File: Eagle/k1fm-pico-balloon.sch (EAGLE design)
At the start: 40 parts, among them Q1 ASTX-H11-25.000MHZ-T, Q2 DMP2305U, Q3 DMP2305U, U1 ATMEGA328, U2 Si5351A-B-GT, U3 MCP1754X-XXXXX/C, U4 TMP36, Y1 8/16/20MHz

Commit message: 4 Layers. Added external SCL, SDA, GPS lines.
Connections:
- new net B0: GPS1.4_TIMEPULSE, U1.PB0(ICP)
- new net D7: U1.PD7(AIN1), U2.CLK2
- net 3V: no longer J3.2
- net GND: no longer J3.1
- net SCL: now also J3.2
- net SDA: now also J3.1
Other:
- note added: "K1FM Pico Balloon 1.3"
- note removed: "K1FM Pico Balloon 1.2"
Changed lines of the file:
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@@
 <?xml version="1.0" encoding="utf-8"?>
 <!DOCTYPE eagle SYSTEM "eagle.dtd">
-<eagle version="9.2.2">
+<eagle version="9.4.1">
 <drawing>
 <settings>
@@
 <sheet>
 <plain>
-<text x="203.2" y="10.16" size="7.62" layer="94">K1FM Pico Balloon 1.2</text>
+<text x="203.2" y="10.16" size="7.62" layer="94">K1FM Pico Balloon 1.3</text>
 </plain>
 <instances>
@@
 </segment>
 <segment>
-<wire x1="38.1" y1="78.74" x2="40.64" y2="78.74" width="0.1524" layer="91"/>
-<label x="40.64" y="78.74" size="1.27" layer="95" xref="yes"/>
-<pinref part="J3" gate="G$1" pin="1"/>
-</segment>
-<segment>
 <pinref part="GPS-ANT" gate="G$1" pin="1"/>
 <pinref part="GND12" gate="1" pin="GND"/>
@@
 </net>
 <net name="3V" class="0">
-<segment>
-<wire x1="38.1" y1="81.28" x2="40.64" y2="81.28" width="0.1524" layer="91"/>
-<label x="40.64" y="81.28" size="1.27" layer="95" xref="yes"/>
-<pinref part="J3" gate="G$1" pin="2"/>
-</segment>
 <segment>
 <pinref part="R4" gate="G$1" pin="1"/>
@@
 <label x="261.62" y="55.88" size="1.27" layer="95" rot="R180" xref="yes"/>
 </segment>
+<segment>
+<wire x1="38.1" y1="78.74" x2="40.64" y2="78.74" width="0.1524" layer="91"/>
+<label x="40.64" y="78.74" size="1.27" layer="95" xref="yes"/>
+<pinref part="J3" gate="G$1" pin="1"/>
+</segment>
 </net>
 <net name="SCL" class="0">
@@
 <label x="261.62" y="58.42" size="1.27" layer="95" rot="R180" xref="yes"/>
 </segment>
+<segment>
+<wire x1="38.1" y1="81.28" x2="40.64" y2="81.28" width="0.1524" layer="91"/>
+<label x="40.64" y="81.28" size="1.27" layer="95" xref="yes"/>
+<pinref part="J3" gate="G$1" pin="2"/>
+</segment>
 </net>
 <net name="CLK0" class="0">
 <segment>
 <pinref part="U2" gate="G$1" pin="CLK0"/>
-<wire x1="289.56" y1="66.04" x2="292.1" y2="66.04" width="0.1524" layer="91"/>
-<label x="292.1" y="66.04" size="1.778" layer="95" xref="yes"/>
+<wire x1="289.56" y1="66.04" x2="294.64" y2="66.04" width="0.1524" layer="91"/>
+<wire x1="294.64" y1="66.04" x2="294.64" y2="68.58" width="0.1524" layer="91"/>
+<label x="294.64" y="68.58" size="1.778" layer="95" rot="R90" xref="yes"/>
 </segment>
 <segment>
@@
 </segment>
 </net>
+<net name="B0" class="0">
+<segment>
+<pinref part="U1" gate="G$1" pin="PB0(ICP)"/>
+<wire x1="157.48" y1="68.58" x2="160.02" y2="68.58" width="0.1524" layer="91"/>
+<label x="160.02" y="68.58" size="1.778" layer="95" xref="yes"/>
+</segment>
+<segment>
+<pinref part="GPS1" gate="G$1" pin="4_TIMEPULSE"/>
+<wire x1="223.52" y1="149.86" x2="226.06" y2="149.86" width="0.1524" layer="91"/>
+<label x="226.06" y="149.86" size="1.778" layer="95" xref="yes"/>
+</segment>
+</net>
+<net name="D7" class="0">
+<segment>
+<pinref part="U1" gate="G$1" pin="PD7(AIN1)"/>
+<wire x1="157.48" y1="73.66" x2="160.02" y2="73.66" width="0.1524" layer="91"/>
+<label x="160.02" y="73.66" size="1.27" layer="95" xref="yes"/>
+</segment>
+<segment>
+<pinref part="U2" gate="G$1" pin="CLK2"/>
+<wire x1="289.56" y1="55.88" x2="292.1" y2="55.88" width="0.1524" layer="91"/>
+<label x="292.1" y="55.88" size="1.27" layer="95" xref="yes"/>
+</segment>
+</net>

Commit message: Reorganized TX/RX lines - Conn layout
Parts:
- added J1: I2C, SparkFun-Connectors:CONN_02
- J2: value (none) -> ICSP; device SparkFun-Connectors:6_PIN_SERIAL_TARGET -> SparkFun-Connectors:CONN_03X2FEMALE
- J3: value (none) -> SERIAL; device SparkFun-Connectors:CONN_06SILK_FEMALE_PTH -> SparkFun-Connectors:CONN_03
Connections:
- net B0 renamed TIMEP
- net D7 renamed CLK2
- removed net D3: GPS1.3_RXD1, U1.PD3(INT1)
- removed net D4: GPS1.2_TXD1, U1.PD4(XCK/T0)
- new net RXD: GPS1.2_TXD1, U1.PD0(RXD)
- new net TXD: GPS1.3_RXD1, U1.PD1(TXD)
- net 3V: now also J2.2; no longer J2.VCC
- net DTR: now also J3.1; no longer J2.DTR
- net GND: now also J2.6; no longer J2.CTS, J2.GND
- net MISO: now also J2.1; no longer J3.5
- net MOSI: now also J2.4; no longer J3.4
- net RESET: now also J2.5; no longer J3.6
- net RXI: now also J3.3, U1.PD3(INT1); no longer J2.TXO, U1.PD0(RXD)
- net SCK: now also J2.3; no longer J3.3
- net SCL: now also J1.2; no longer J3.2
- net SDA: now also J1.1; no longer J3.1
- net TXO: now also J3.2, U1.PD4(XCK/T0); no longer J2.RXI, U1.PD1(TXD)
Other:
- note added: "K1FM Pico Balloon 1.3 WORK IN PROGRESS"
- note removed: "K1FM Pico Balloon 1.3"
- moved on the sheet: C10, J2

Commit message: Add diode and connection for direct solar power
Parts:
- removed 3.3V: 3.3V, SparkFun-Connectors:CONN_02
- added D1: 1N4148X-TP, diode:DIODE-SOD523
- added J4: POWER, SparkFun-Connectors:CONN_03
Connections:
- new net N$3: D1.A, J4.3
- net GND: now also J4.2; no longer 3.3V.2
- net VDD: now also D1.C, J4.1; no longer 3.3V.1
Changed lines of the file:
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@@
 <part name="GND6" library="SparkFun" deviceset="GND" device=""/>
 <part name="C11" library="SparkFun-Capacitors" library_urn="urn:adsk.eagle:library:510" deviceset="0.1UF" device="-0603-25V-5%" package3d_urn="urn:adsk.eagle:package:37414/1" value="0.47uF"/>
-<part name="3.3V" library="SparkFun-Connectors" library_urn="urn:adsk.eagle:library:513" deviceset="CONN_02" device="" package3d_urn="urn:adsk.eagle:package:38039/1" value="3.3V"/>
 <part name="R3" library="SparkFun-Resistors" library_urn="urn:adsk.eagle:library:532" deviceset="4.7KOHM" device="-0603-1/10W-1%" package3d_urn="urn:adsk.eagle:package:39650/1" value="4.7k"/>
 <part name="R4" library="SparkFun-Resistors" library_urn="urn:adsk.eagle:library:532" deviceset="4.7KOHM" device="-0603-1/10W-1%" package3d_urn="urn:adsk.eagle:package:39650/1" value="4.7k"/>
@@
 <part name="J2" library="SparkFun-Connectors" library_urn="urn:adsk.eagle:library:513" deviceset="CONN_03X2" device="FEMALE" package3d_urn="urn:adsk.eagle:package:38016/1" value="ICSP"/>
 <part name="J3" library="SparkFun-Connectors" library_urn="urn:adsk.eagle:library:513" deviceset="CONN_03" device="" package3d_urn="urn:adsk.eagle:package:38063/1" value="SERIAL"/>
+<part name="D1" library="diode" library_urn="urn:adsk.eagle:library:210" deviceset="DIODE-" device="SOD523" package3d_urn="urn:adsk.eagle:package:43410/1" value="1N4148X-TP"/>
+<part name="J4" library="SparkFun-Connectors" library_urn="urn:adsk.eagle:library:513" deviceset="CONN_03" device="" package3d_urn="urn:adsk.eagle:package:38063/1" value="POWER"/>
 </parts>
 <sheets>
@@
 <attribute name="VALUE" x="306.324" y="48.641" size="1.778" layer="96" font="vector"/>
 </instance>
-<instance part="3.3V" gate="G$1" x="35.56" y="177.8" smashed="yes" rot="R270">
-<attribute name="VALUE" x="30.734" y="180.34" size="1.778" layer="96" font="vector" rot="R270"/>
-<attribute name="NAME" x="41.148" y="180.34" size="1.778" layer="95" font="vector" rot="R270"/>
-</instance>
 <instance part="R3" gate="G$1" x="172.72" y="111.76" smashed="yes" rot="R90">
 <attribute name="NAME" x="171.196" y="111.76" size="1.778" layer="95" font="vector" rot="R90" align="bottom-center"/>
@@
 <attribute name="VALUE" x="30.48" y="78.994" size="1.778" layer="96" font="vector"/>
 <attribute name="NAME" x="30.48" y="91.948" size="1.778" layer="95" font="vector"/>
+</instance>
+<instance part="D1" gate="G$1" x="27.94" y="177.8" smashed="yes" rot="R270">
+<attribute name="NAME" x="28.4226" y="175.26" size="1.778" layer="95" rot="R270"/>
+<attribute name="VALUE" x="25.6286" y="175.26" size="1.778" layer="96" rot="R270"/>
+</instance>
+<instance part="J4" gate="J$1" x="38.1" y="177.8" smashed="yes" rot="R270">
+<attribute name="VALUE" x="30.734" y="180.34" size="1.778" layer="96" font="vector" rot="R270"/>
+<attribute name="NAME" x="43.688" y="180.34" size="1.778" layer="95" font="vector" rot="R270"/>
 </instance>
 </instances>
@@
 <pinref part="GND1" gate="1" pin="GND"/>
 <wire x1="38.1" y1="167.64" x2="38.1" y2="170.18" width="0.1524" layer="91"/>
-<pinref part="3.3V" gate="G$1" pin="2"/>
+<pinref part="J4" gate="J$1" pin="2"/>
 </segment>
 <segment>
@@
 <segment>
 <wire x1="35.56" y1="167.64" x2="35.56" y2="170.18" width="0.1524" layer="91"/>
-<pinref part="3.3V" gate="G$1" pin="1"/>
-<label x="33.02" y="167.64" size="1.778" layer="95" rot="R180" xref="yes"/>
-<wire x1="33.02" y1="167.64" x2="35.56" y2="167.64" width="0.1524" layer="91"/>
+<label x="25.4" y="167.64" size="1.778" layer="95" rot="R180" xref="yes"/>
+<wire x1="25.4" y1="167.64" x2="27.94" y2="167.64" width="0.1524" layer="91"/>
+<pinref part="D1" gate="G$1" pin="C"/>
+<wire x1="27.94" y1="167.64" x2="35.56" y2="167.64" width="0.1524" layer="91"/>
+<wire x1="27.94" y1="175.26" x2="27.94" y2="167.64" width="0.1524" layer="91"/>
+<junction x="27.94" y="167.64"/>
+<pinref part="J4" gate="J$1" pin="1"/>
 </segment>
 <segment>
@@
 </segment>
 </net>
+<net name="N$3" class="0">
+<segment>
+<pinref part="D1" gate="G$1" pin="A"/>
+<wire x1="27.94" y1="180.34" x2="27.94" y2="185.42" width="0.1524" layer="91"/>
+<wire x1="27.94" y1="185.42" x2="48.26" y2="185.42" width="0.1524" layer="91"/>
+<wire x1="48.26" y1="185.42" x2="48.26" y2="167.64" width="0.1524" layer="91"/>
+<wire x1="48.26" y1="167.64" x2="40.64" y2="167.64" width="0.1524" layer="91"/>
+<pinref part="J4" gate="J$1" pin="3"/>
+<wire x1="40.64" y1="167.64" x2="40.64" y2="170.18" width="0.1524" layer="91"/>
+</segment>
+</net>

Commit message: Revert to classic hw/sw serial configuration
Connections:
- net RXD: now also J3.3; no longer GPS1.2_TXD1
- net RXI: now also GPS1.2_TXD1, U1.PD4(XCK/T0); no longer J3.3, U1.PD3(INT1)
- net TXD: now also J3.2; no longer GPS1.3_RXD1
- net TXO: now also GPS1.3_RXD1, U1.PD3(INT1); no longer J3.2, U1.PD4(XCK/T0)
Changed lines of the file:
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@@
-</segment>
-</net>
-<net name="TXO" class="0">
-<segment>
-<pinref part="U1" gate="G$1" pin="PD4(XCK/T0)"/>
-<wire x1="157.48" y1="81.28" x2="160.02" y2="81.28" width="0.1524" layer="91"/>
-<label x="160.02" y="81.28" size="1.27" layer="95" xref="yes"/>
-</segment>
-<segment>
-<pinref part="J3" gate="J$1" pin="2"/>
-<wire x1="40.64" y1="86.36" x2="43.18" y2="86.36" width="0.1524" layer="91"/>
-<label x="43.18" y="86.36" size="1.27" layer="95" xref="yes"/>
-</segment>
-</net>
-<net name="RXI" class="0">
-<segment>
-<pinref part="U1" gate="G$1" pin="PD3(INT1)"/>
-<wire x1="157.48" y1="83.82" x2="160.02" y2="83.82" width="0.1524" layer="91"/>
-<label x="160.02" y="83.82" size="1.27" layer="95" xref="yes"/>
-</segment>
-<segment>
-<pinref part="J3" gate="J$1" pin="3"/>
-<wire x1="40.64" y1="88.9" x2="43.18" y2="88.9" width="0.1524" layer="91"/>
-<label x="43.18" y="88.9" size="1.27" layer="95" xref="yes"/>
 </segment>
 </net>
@@
 </segment>
 <segment>
-<pinref part="GPS1" gate="G$1" pin="2_TXD1"/>
-<wire x1="223.52" y1="139.7" x2="226.06" y2="139.7" width="0.1524" layer="91"/>
-<label x="226.06" y="139.7" size="1.778" layer="95" xref="yes"/>
+<pinref part="J3" gate="J$1" pin="3"/>
+<wire x1="40.64" y1="88.9" x2="43.18" y2="88.9" width="0.1524" layer="91"/>
+<label x="43.18" y="88.9" size="1.27" layer="95" xref="yes"/>
 </segment>
 </net>
@@
 </segment>
 <segment>
-<wire x1="226.06" y1="144.78" x2="223.52" y2="144.78" width="0.1524" layer="91"/>
-<pinref part="GPS1" gate="G$1" pin="3_RXD1"/>
-<label x="226.06" y="144.78" size="1.778" layer="95" xref="yes"/>
+<pinref part="J3" gate="J$1" pin="2"/>
+<wire x1="40.64" y1="86.36" x2="43.18" y2="86.36" width="0.1524" layer="91"/>
+<label x="43.18" y="86.36" size="1.27" layer="95" xref="yes"/>
 </segment>
 </net>
@@
 </segment>
 </net>
+<net name="RXI" class="0">
+<segment>
+<pinref part="U1" gate="G$1" pin="PD4(XCK/T0)"/>
+<wire x1="157.48" y1="81.28" x2="160.02" y2="81.28" width="0.1524" layer="91"/>
+<label x="160.02" y="81.28" size="1.27" layer="95" xref="yes"/>
+</segment>
+<segment>
+<pinref part="GPS1" gate="G$1" pin="2_TXD1"/>
+<wire x1="223.52" y1="139.7" x2="226.06" y2="139.7" width="0.1524" layer="91"/>
+<label x="226.06" y="139.7" size="1.778" layer="95" xref="yes"/>
+</segment>
+</net>
+<net name="TXO" class="0">
+<segment>
+<pinref part="U1" gate="G$1" pin="PD3(INT1)"/>
+<wire x1="157.48" y1="83.82" x2="160.02" y2="83.82" width="0.1524" layer="91"/>
+<label x="160.02" y="83.82" size="1.27" layer="95" xref="yes"/>
+</segment>
+<segment>
+<pinref part="GPS1" gate="G$1" pin="3_RXD1"/>
+<wire x1="223.52" y1="144.78" x2="226.06" y2="144.78" width="0.1524" layer="91"/>
+<label x="226.06" y="144.78" size="1.778" layer="95" xref="yes"/>
+</segment>
+</net>

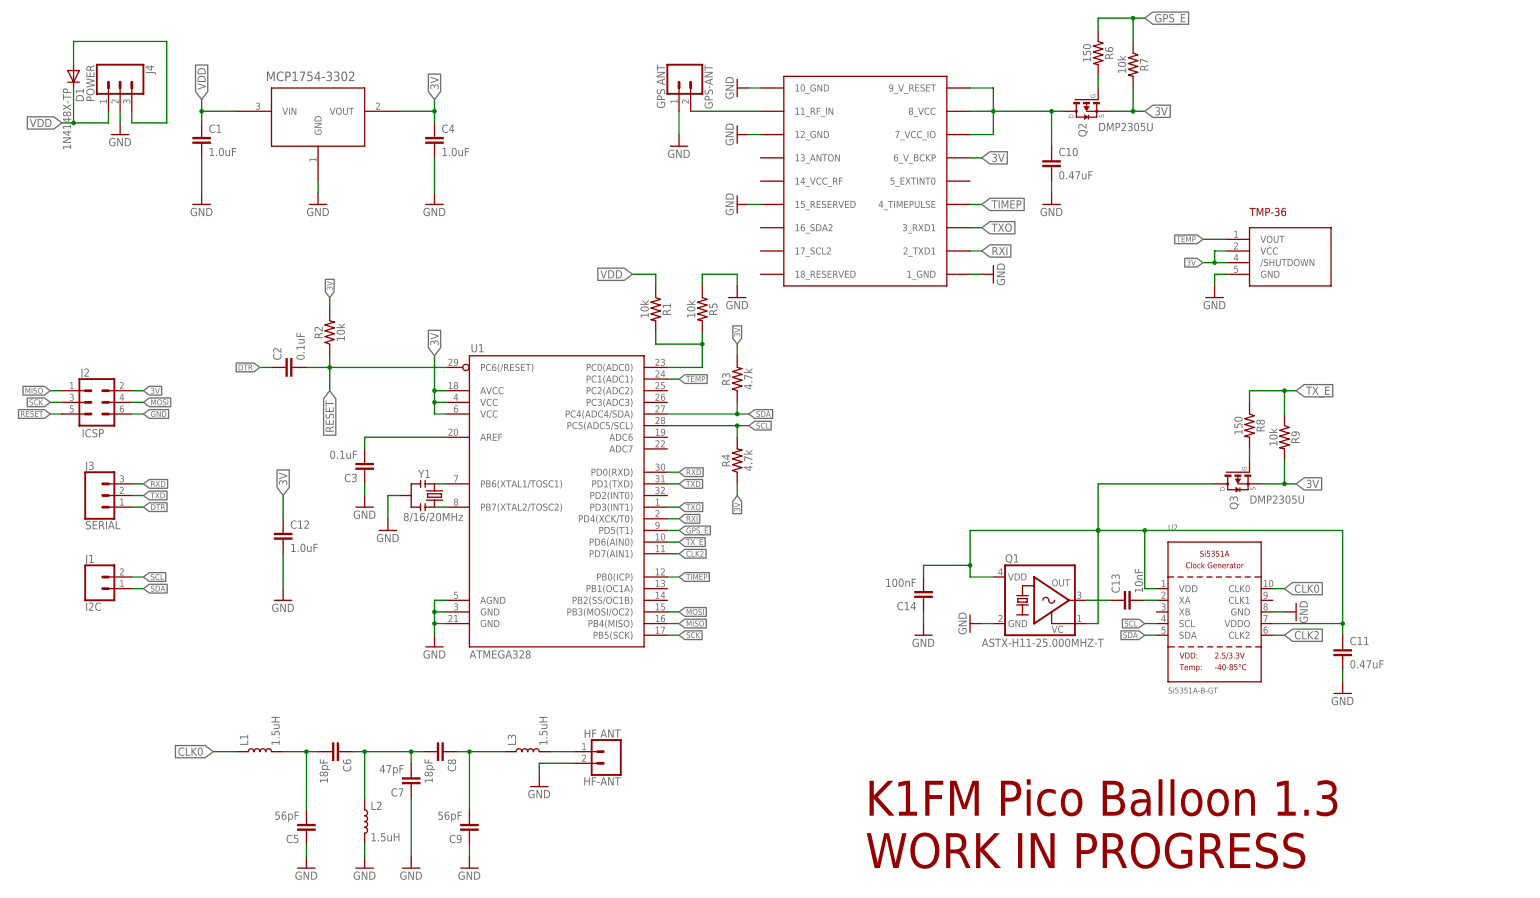
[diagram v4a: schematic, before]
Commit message: Redraw VDD measure input
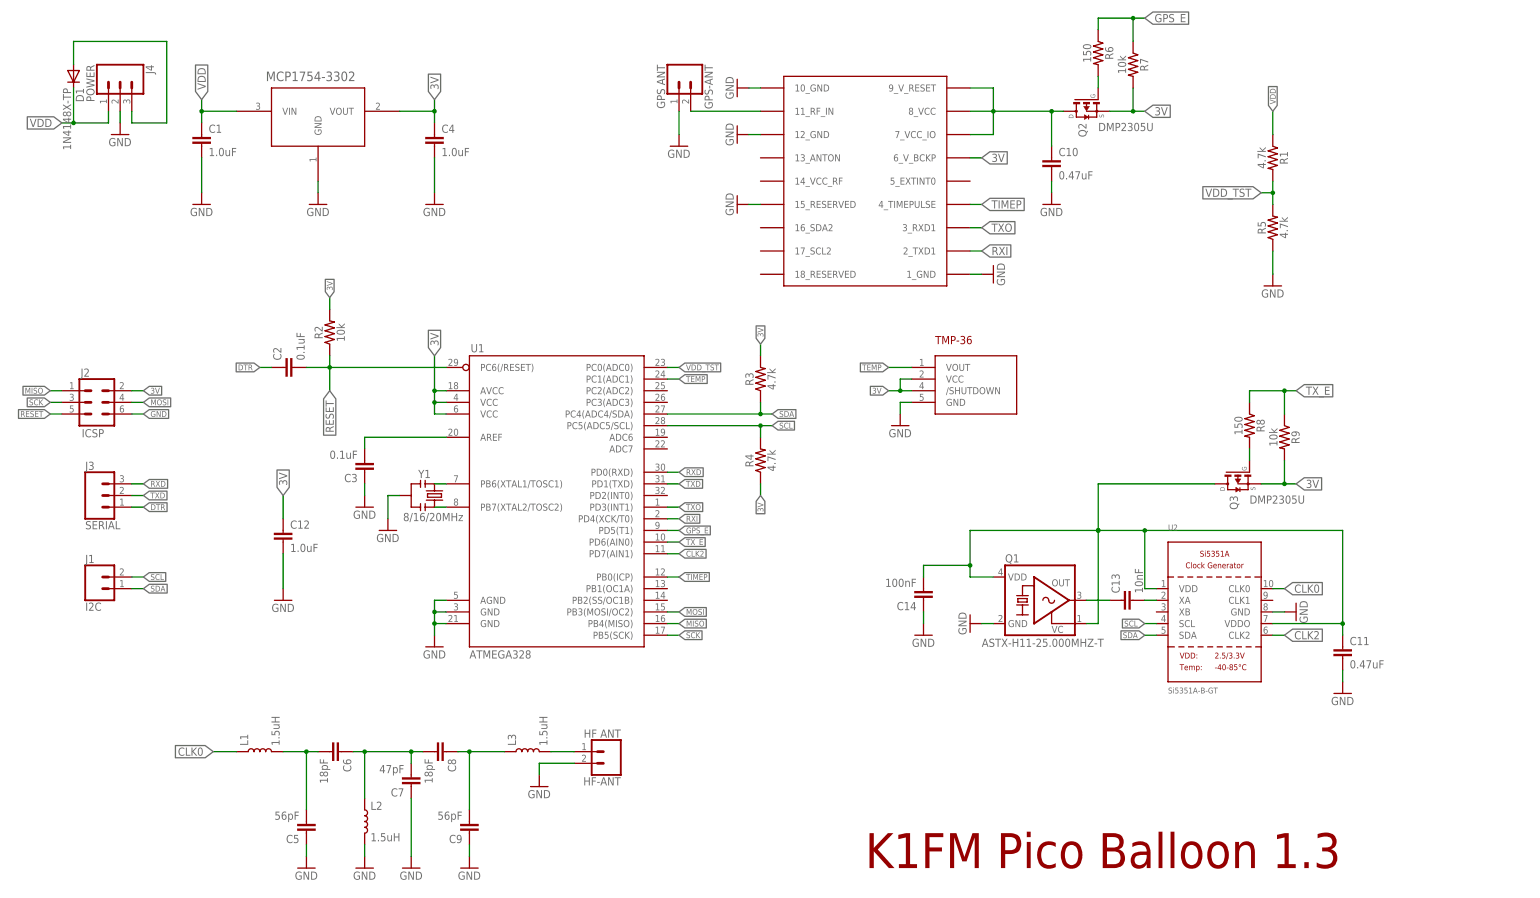
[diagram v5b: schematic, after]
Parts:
- R1, R5: value 10k -> 4.7k
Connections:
- net N$4 renamed VDD_TST
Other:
- note added: "K1FM Pico Balloon 1.3"
- note removed: "K1FM Pico Balloon 1.3 WORK IN PROGRESS"
- moved on the sheet: R1, R3, R4, R5

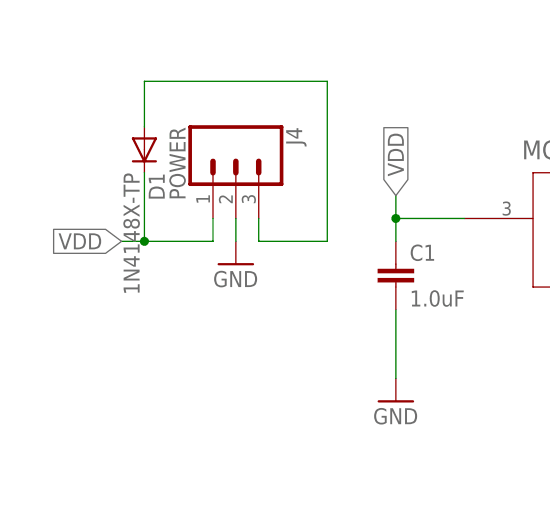
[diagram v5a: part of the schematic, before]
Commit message: Use diode BAT20J, space out break lines, bugfix
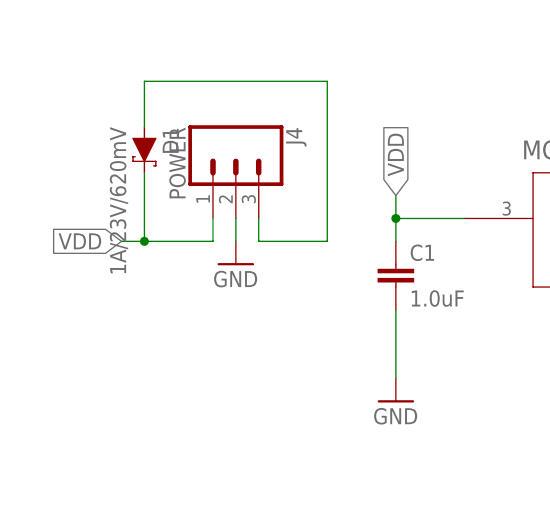
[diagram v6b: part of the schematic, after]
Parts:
- D1: value 1N4148X-TP -> 1A/23V/620mV; device diode:DIODE-SOD523 -> SparkFun-DiscreteSemi:DIODE-SCHOTTKY-BAT20J
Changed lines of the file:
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@@
 <part name="J2" library="SparkFun-Connectors" library_urn="urn:adsk.eagle:library:513" deviceset="CONN_03X2" device="FEMALE" package3d_urn="urn:adsk.eagle:package:38016/1" value="ICSP"/>
 <part name="J3" library="SparkFun-Connectors" library_urn="urn:adsk.eagle:library:513" deviceset="CONN_03" device="" package3d_urn="urn:adsk.eagle:package:38063/1" value="SERIAL"/>
-<part name="D1" library="diode" library_urn="urn:adsk.eagle:library:210" deviceset="DIODE-" device="SOD523" package3d_urn="urn:adsk.eagle:package:43410/1" value="1N4148X-TP"/>
 <part name="J4" library="SparkFun-Connectors" library_urn="urn:adsk.eagle:library:513" deviceset="CONN_03" device="" package3d_urn="urn:adsk.eagle:package:38063/1" value="POWER"/>
+<part name="D1" library="SparkFun-DiscreteSemi" library_urn="urn:adsk.eagle:library:514" deviceset="DIODE-SCHOTTKY" device="-BAT20J" package3d_urn="urn:adsk.eagle:package:38441/1" value="1A/23V/620mV"/>
 </parts>
 <sheets>
@@
 <attribute name="NAME" x="30.48" y="91.948" size="1.778" layer="95" font="vector"/>
 </instance>
-<instance part="D1" gate="G$1" x="27.94" y="177.8" smashed="yes" rot="R270">
-<attribute name="NAME" x="28.4226" y="175.26" size="1.778" layer="95" rot="R270"/>
-<attribute name="VALUE" x="25.6286" y="175.26" size="1.778" layer="96" rot="R270"/>
-</instance>
 <instance part="J4" gate="J$1" x="38.1" y="177.8" smashed="yes" rot="R270">
 <attribute name="VALUE" x="30.734" y="180.34" size="1.778" layer="96" font="vector" rot="R270"/>
 <attribute name="NAME" x="43.688" y="180.34" size="1.778" layer="95" font="vector" rot="R270"/>
+</instance>
+<instance part="D1" gate="G$1" x="27.94" y="177.8" smashed="yes" rot="R270">
+<attribute name="NAME" x="29.972" y="180.34" size="1.778" layer="95" font="vector" rot="R270"/>
+<attribute name="VALUE" x="25.908" y="180.34" size="1.778" layer="96" font="vector" rot="R270" align="top-left"/>
 </instance>
 </instances>
@@
 <label x="25.4" y="167.64" size="1.778" layer="95" rot="R180" xref="yes"/>
 <wire x1="25.4" y1="167.64" x2="27.94" y2="167.64" width="0.1524" layer="91"/>
-<pinref part="D1" gate="G$1" pin="C"/>
 <wire x1="27.94" y1="167.64" x2="35.56" y2="167.64" width="0.1524" layer="91"/>
 <wire x1="27.94" y1="175.26" x2="27.94" y2="167.64" width="0.1524" layer="91"/>
 <junction x="27.94" y="167.64"/>
 <pinref part="J4" gate="J$1" pin="1"/>
+<pinref part="D1" gate="G$1" pin="C"/>
 </segment>
 <segment>
@@
 <net name="N$3" class="0">
 <segment>
-<pinref part="D1" gate="G$1" pin="A"/>
 <wire x1="27.94" y1="180.34" x2="27.94" y2="185.42" width="0.1524" layer="91"/>
 <wire x1="27.94" y1="185.42" x2="48.26" y2="185.42" width="0.1524" layer="91"/>
@@
 <pinref part="J4" gate="J$1" pin="3"/>
 <wire x1="40.64" y1="167.64" x2="40.64" y2="170.18" width="0.1524" layer="91"/>
-</segment>
-</net>
+<pinref part="D1" gate="G$1" pin="A"/>
+</segment>
+</net>
